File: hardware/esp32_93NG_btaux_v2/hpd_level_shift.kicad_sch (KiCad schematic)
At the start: 6 parts, among them U1 SN65HVD230, U2 SN65HVD230

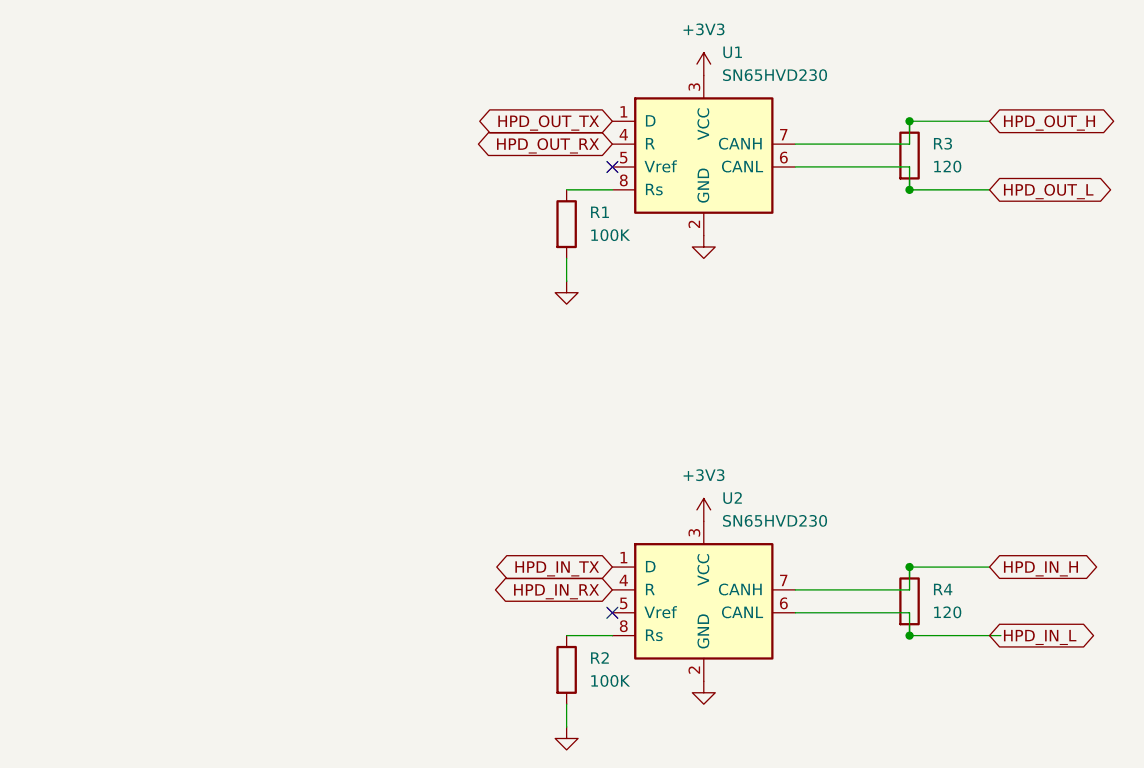
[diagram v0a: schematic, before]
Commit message: Adjusted silkscreen labels to reduce clutter. Added GPIO header for external buttons or LEDs. Added second PCB faceplate, for the bottom-side of the assembly.
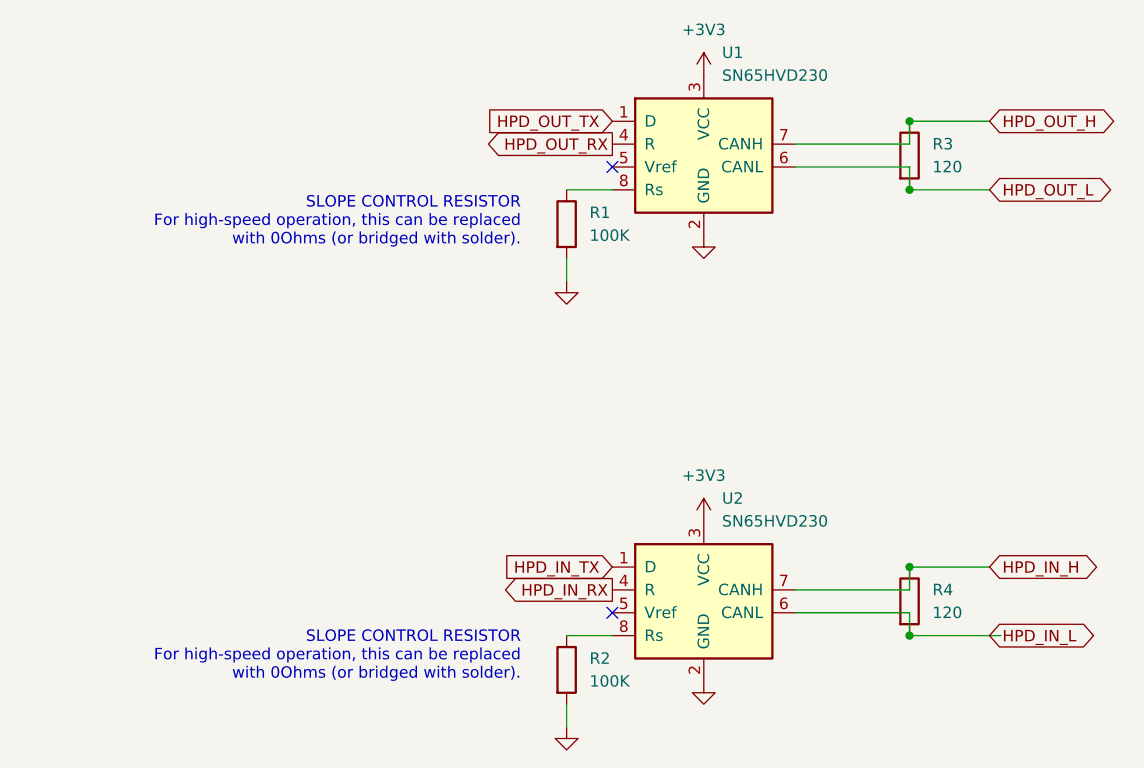
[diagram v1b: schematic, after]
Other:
- note added: "SLOPE CONTROL RESISTOR For high-speed operation, this can be replaced with 0Ohms (or bridged with solder)."
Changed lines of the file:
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@@
     (stroke (width 0) (type default) (color 0 0 0 0))
   )
-  (global_label "HPD_OUT_TX" (shape bidirectional) (at 129.54 57.15 180) (fields_autoplaced)
+  (text "SLOPE CONTROL RESISTOR\nFor high-speed operation, this can be replaced \nwith 0Ohms (or bridged with solder)."
+    (at 119.38 119.38 0)
+    (effects (font (size 1.27 1.27)) (justify right bottom))
+  )
+  (text "SLOPE CONTROL RESISTOR\nFor high-speed operation, this can be replaced \nwith 0Ohms (or bridged with solder)."
+    (at 119.38 71.12 0)
+    (effects (font (size 1.27 1.27)) (justify right bottom))
+  )
+  (global_label "HPD_OUT_TX" (shape input) (at 129.54 57.15 180) (fields_autoplaced)
     (effects (font (size 1.27 1.27)) (justify right))
     (property "Intersheet References" "${INTERSHEET_REFS}" (id 0) (at 115.5155 57.0706 0)
@@
     )
   )
-  (global_label "HPD_OUT_RX" (shape bidirectional) (at 129.54 59.69 180) (fields_autoplaced)
+  (global_label "HPD_OUT_RX" (shape output) (at 129.54 59.69 180) (fields_autoplaced)
     (effects (font (size 1.27 1.27)) (justify right))
     (property "Intersheet References" "${INTERSHEET_REFS}" (id 0) (at 115.2131 59.6106 0)
@@
     )
   )
-  (global_label "HPD_IN_RX" (shape bidirectional) (at 129.54 109.22 180) (fields_autoplaced)
+  (global_label "HPD_IN_RX" (shape output) (at 129.54 109.22 180) (fields_autoplaced)
     (effects (font (size 1.27 1.27)) (justify right))
-    (property "Intersheet References" "${INTERSHEET_REFS}" (id 0) (at 116.9064 109.2994 0)
+    (property "Intersheet References" "${INTERSHEET_REFS}" (id 0) (at 116.9064 109.1406 0)
       (effects (font (size 1.27 1.27)) (justify right) hide)
     )
@@
     )
   )
-  (global_label "HPD_IN_TX" (shape bidirectional) (at 129.54 106.68 180) (fields_autoplaced)
+  (global_label "HPD_IN_TX" (shape input) (at 129.54 106.68 180) (fields_autoplaced)
     (effects (font (size 1.27 1.27)) (justify right))
-    (property "Intersheet References" "${INTERSHEET_REFS}" (id 0) (at 117.2088 106.7594 0)
+    (property "Intersheet References" "${INTERSHEET_REFS}" (id 0) (at 117.2088 106.6006 0)
       (effects (font (size 1.27 1.27)) (justify right) hide)
     )
